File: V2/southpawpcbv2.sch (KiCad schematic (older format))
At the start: 206 parts, among them J1 AVR-ISP-6, SW1 Reset, U1 ATmega32U4-AU, Y1 16MHz

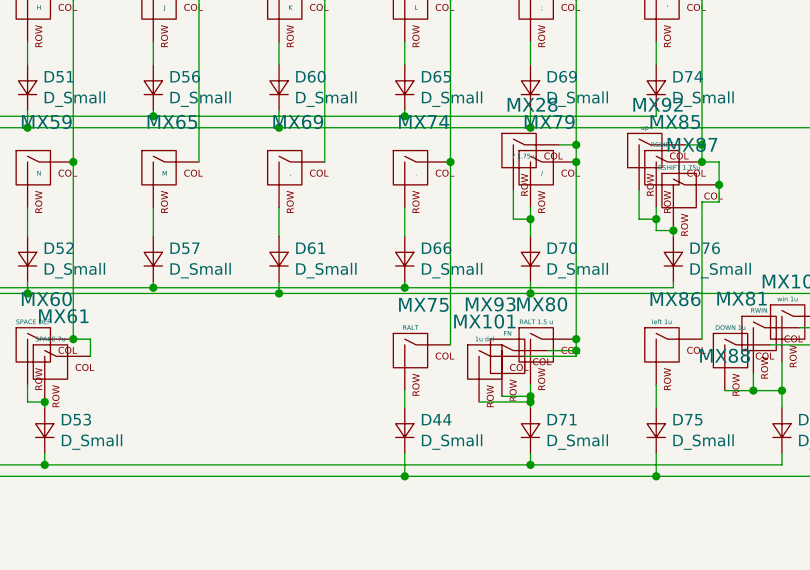
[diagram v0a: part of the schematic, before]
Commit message: fixed crucial errors on both PCBS
added and fixed gerbers/bom/pos for all
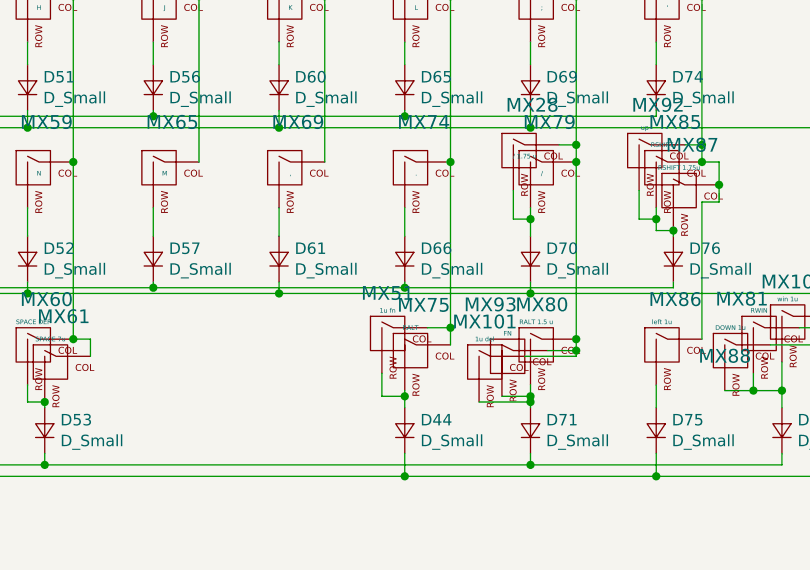
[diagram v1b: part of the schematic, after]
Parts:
- added MX51: 1u fn, MX_Only:MXOnly-1U-NoLED, symbol MX_Alps_Hybrid:MX-NoLED
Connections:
- net col6: now also MX51.1 (COL)
- net at D44.2 (A), MX75.2 (ROW): now also MX51.2 (ROW)
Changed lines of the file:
@@
 	2250 11100 2250 11800
 Wire Wire Line
-	8300 11075 8300 11875
+	8300 11075 8300 11800
 Connection ~ 8300 11075
 $Comp
@@
 $EndComp
 Wire Wire Line
-	8100 12075 8100 12150
+	8100 12075 8100 12100
 Wire Wire Line
 	9950 9600 9950 11750
@@
 	1    0    0    -1
 $EndComp
+$Comp
+L MX_Alps_Hybrid:MX-NoLED MX51
+U 1 1 5F833296
+P 8050 11850
+F 0 "MX51" H 8025 12050 60  0000 C CNN
+F 1 "1u fn" H 8025 11975 20  0000 C CNN
+F 2 "MX_Only:MXOnly-1U-NoLED" H 7425 11825 60  0001 C CNN
+F 3 "" H 7425 11825 60  0001 C CNN
+	1    8050 11850
+	1    0    0    -1
+$EndComp
+Wire Wire Line
+	8200 11800 8300 11800
+Connection ~ 8300 11800
+Wire Wire Line
+	8300 11800 8300 11875
+Wire Wire Line
+	8000 12000 8000 12100
+Wire Wire Line
+	8000 12100 8100 12100
+Connection ~ 8100 12100
+Wire Wire Line
+	8100 12100 8100 12150
 $EndSCHEMATC
